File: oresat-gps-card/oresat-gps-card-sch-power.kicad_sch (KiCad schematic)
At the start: 97 parts, among them Q1 DMP2240UDM, Q2 PMV45EN, Q3 DMP3050LVT-7, Q4 DMP3050LVT-7, Q5 PMV45EN, U2 MAX7310ATE, U3 MIC842LYC5, U4 MIC842LYC5, U5 MAX4211FETE, U6 LTC3624, U7 TS5A21366

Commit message: Routine Push
First attempt to clean up schematic
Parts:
- added C51: 10n, Capacitor_SMD:C_1210_3225Metric, symbol Device:C
- added C52: 470n, Capacitor_SMD:C_1210_3225Metric, symbol Device:C
- added R49, R50: 10k, Resistor_SMD:R_0603_1608Metric, symbol Device:R_US
- R24: value 4.7k -> 2.7k
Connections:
- net CB_CTRL: now also R49.1; no longer Q4.3 (G), R39.1
- net VBUSP: now also C52.1
- net at Q4.4 (S), R32.2, R39.2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: now also C51.1
- new net: C51.2, Q4.3 (G), R39.1, R49.2, R50.2
- new net: C52.2, R50.1
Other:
- note added: "Do we need this?"
- moved on the sheet: Q5, R39, R40

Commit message: Routine Push
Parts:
- added D11: GREEN, LED_SMD:LED_0603_1608Metric, symbol Device:LED
- added R61: 10k, Resistor_SMD:R_0603_1608Metric, symbol Device:R_US
- C1, C2, C8: footprint Capacitor_SMD:C_0805_2012Metric -> Capacitor_SMD:C_0603_1608Metric
- C13, C14, C51, C52, C6: footprint Capacitor_SMD:C_1210_3225Metric -> Capacitor_SMD:C_0603_1608Metric
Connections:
- net GND: now also D11.1 (K)
- net ON/~{OFF}: now also R61.1
- new net: D11.2 (A), R61.2
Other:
- note added: "All resistors are 0603 1% AEC-Q200 unless marked. All capacitors are 0603 AEC-Q200 Vw >= 16V X5R or better unless marked."
- note added: "Main Power Switch Vbus = (6.0,7.2,8.4)V"
- note added: "OreSat Power Domain (OPD) Power Supply (3.3V) Address 0011001 or 19"
- note removed: "Main Power Switch"
- note removed: "OreSat Power Domain (OPD) Controller"
- note removed: "OreSat Power Domain (OPD) Power Supply (3.3V)"
- note removed: "Vbus = (6.0,7.2,8.4)V"

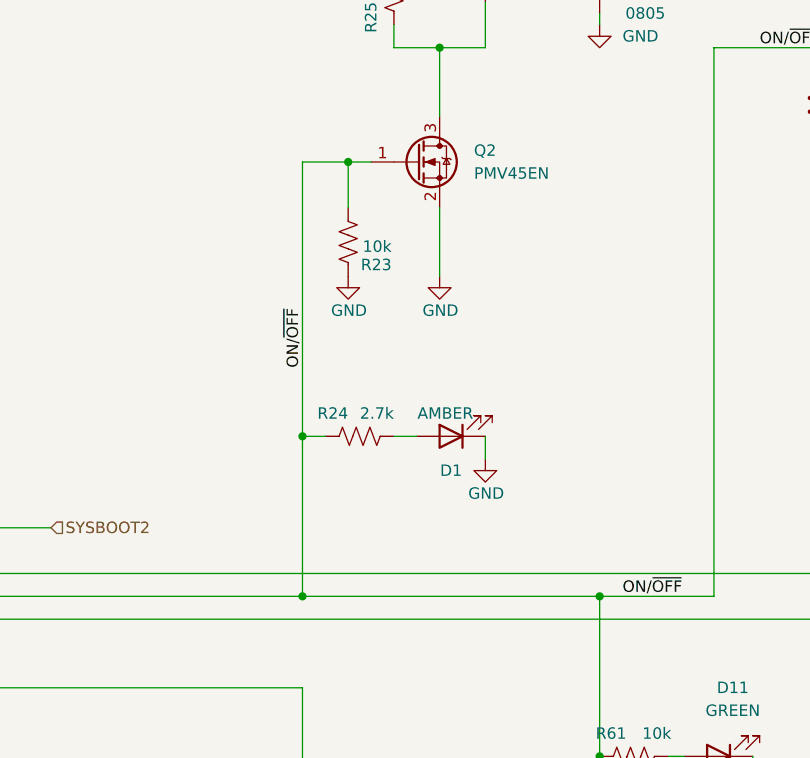
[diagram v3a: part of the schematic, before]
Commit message: Cleaned up silkscreen
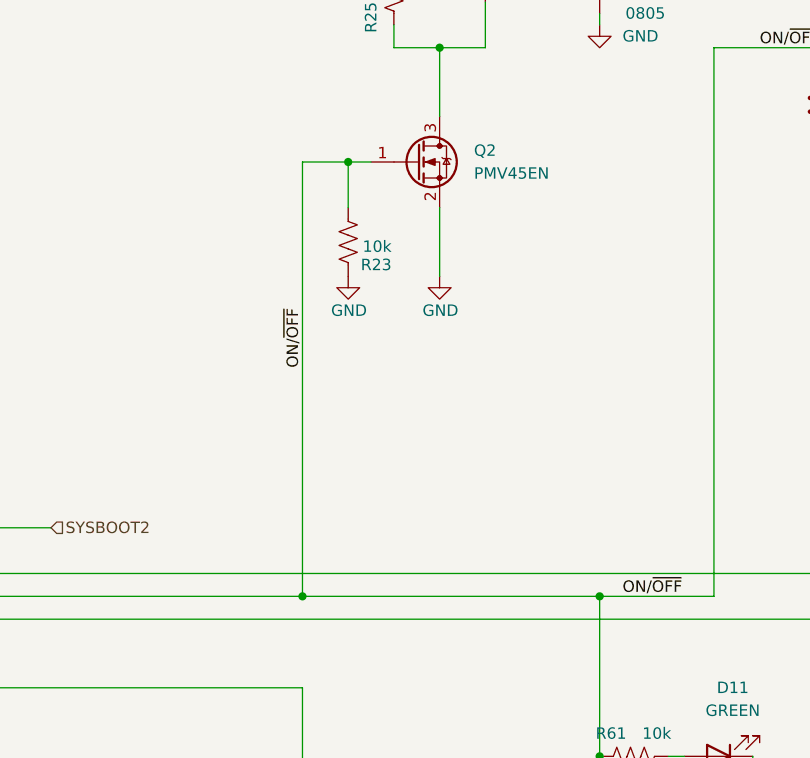
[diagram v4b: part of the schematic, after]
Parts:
- removed D1: AMBER, LED_SMD:LED_0603_1608Metric, symbol Device:LED
- removed R24: 2.7k, Resistor_SMD:R_0603_1608Metric, symbol Device:R_US

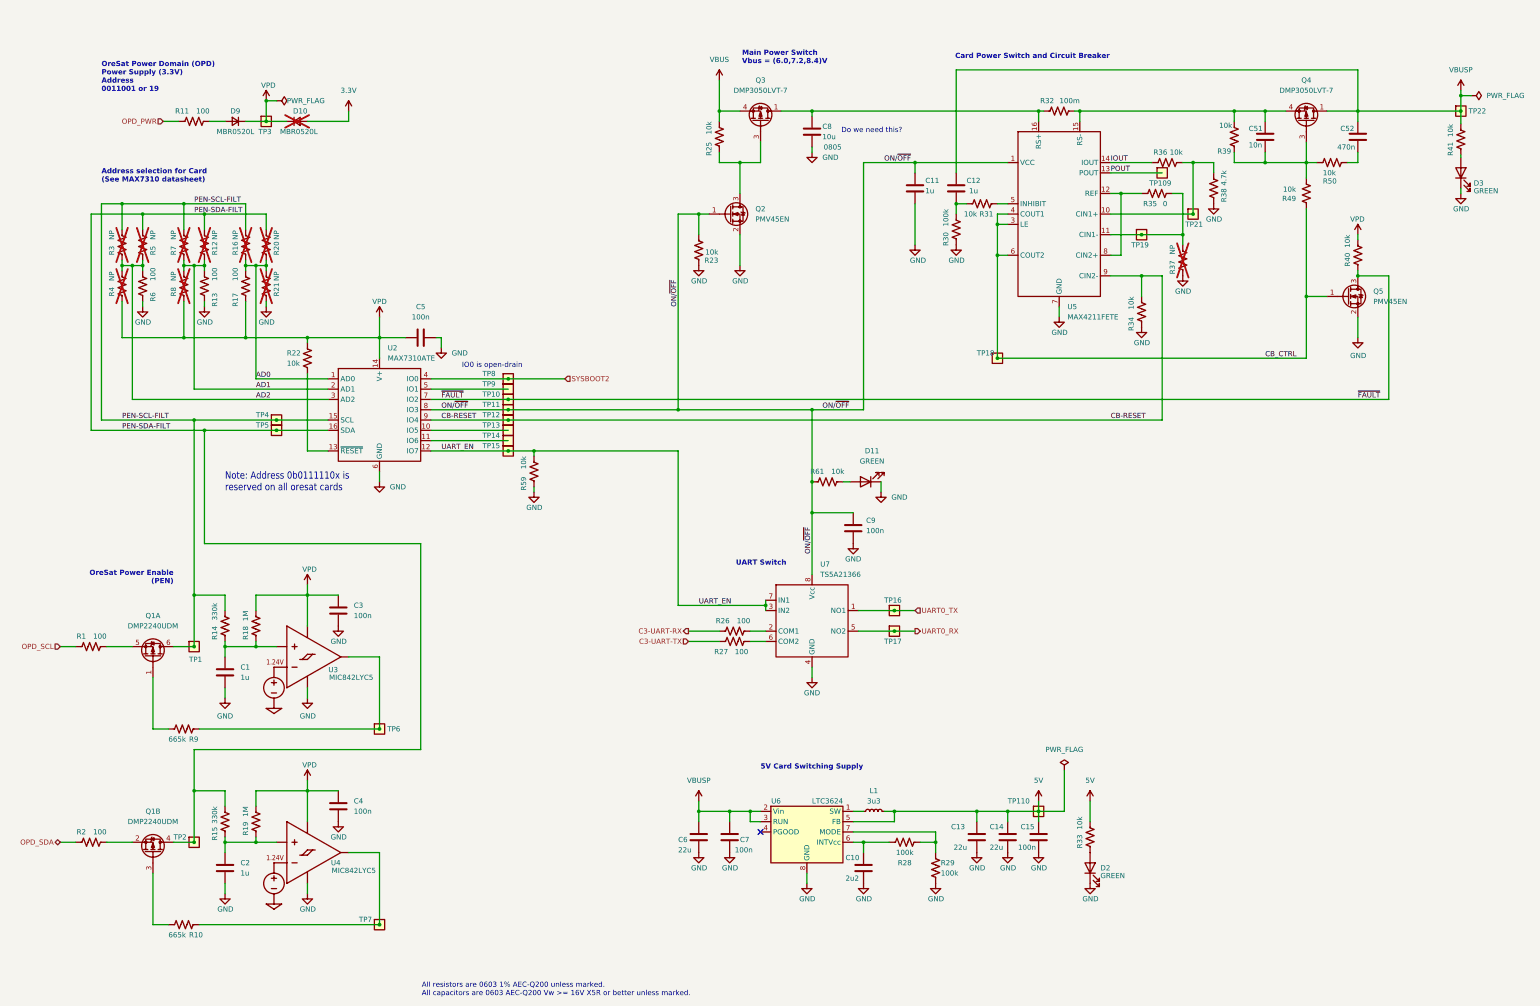
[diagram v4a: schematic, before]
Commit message: General cleanup of schematic and layout
Updated .gitignore, updates DRU file, moved RF lines to RF-50-MIN (max is just too big),
lots of cleanup on the root page to make it pretty, cleaned up some redudant labels,
updated SMPM connector and added rule zone, updated PCB outline to include NPTH drills
for SMPM connectors, began cleanup of OPD.
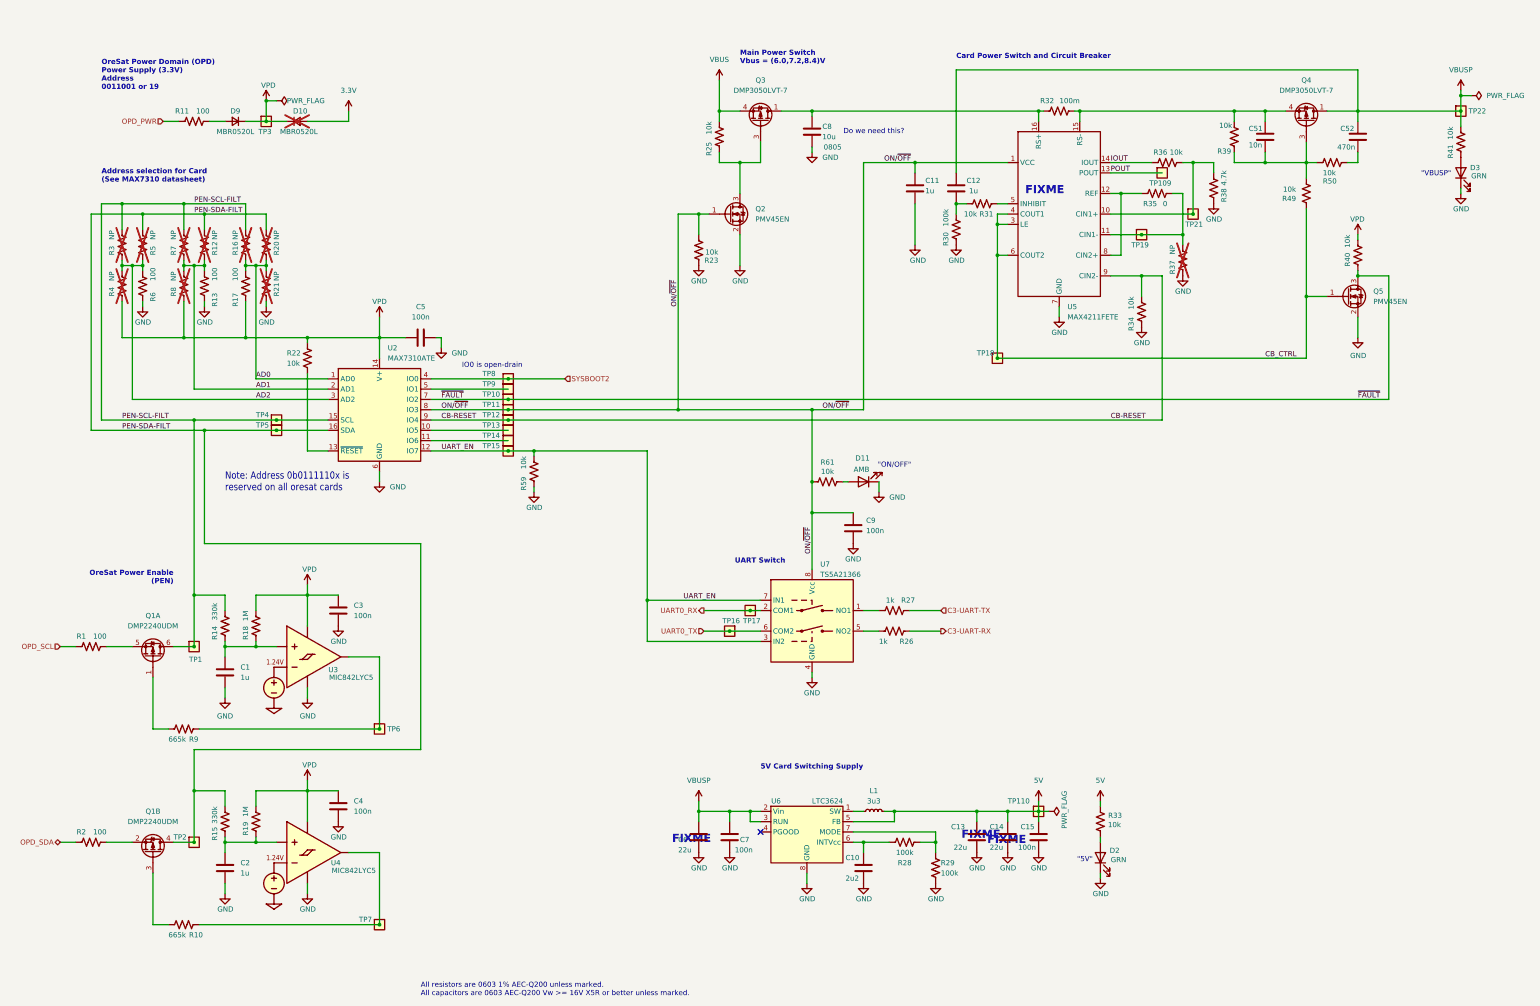
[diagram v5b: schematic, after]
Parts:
- D11: value GREEN -> AMB
- D2, D3: value GREEN -> GRN
- R26, R27: value 100 -> 1k
- U7: DIS (none) -> DigiKey; DPN (none) -> 296-24304-1-ND; MFR (none) -> Texas Instruments; MPN (none) -> TS5A21366DCUR
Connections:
- net UART0_RX: now also U7.2 (COM1); no longer U7.5 (NO2)
- net UART0_TX: now also U7.6 (COM2); no longer U7.1 (NO1)
- net at R26.2: now also U7.5 (NO2); no longer U7.2 (COM1)
- net at R27.1: now also U7.1 (NO1); no longer U7.6 (COM2)
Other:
- note added: ""5V""
- note added: ""ON/OFF""
- note added: ""VBUSP""
- note added: "FIXME"
- moved on the sheet: D11, D2, R26, R27, R33, R41, TP16, TP17

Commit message: Routine Push
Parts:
- removed C11, C12: 1u, Capacitor_SMD:C_0603_1608Metric, symbol Device:C
- removed C13, C14, C6: 22u, Capacitor_SMD:C_0603_1608Metric, symbol Device:C
- removed C51: 10n, Capacitor_SMD:C_0603_1608Metric, symbol Device:C
- removed C52: 470n, Capacitor_SMD:C_0603_1608Metric, symbol Device:C
- removed C8: 10u, Capacitor_SMD:C_0603_1608Metric, symbol Device:C
- removed C9: 100n, Capacitor_SMD:C_0603_1608Metric, symbol Device:C
- removed D11: AMB, LED_SMD:LED_0603_1608Metric, symbol Device:LED
- removed D3: GRN, LED_SMD:LED_0603_1608Metric, symbol Device:LED
- removed Q2, Q5: PMV45EN, oresat-ics:SOT23, symbol Device:Q_NMOS_GSD
- removed Q3, Q4: DMP3050LVT-7, Package_TO_SOT_SMD:SOT-23-6, symbol oresat-transistors:DMP3050LVT-7
- removed R23, R25, R31, R34, R36, R39, R40, R41, R49, R50, R61: 10k, Resistor_SMD:R_0603_1608Metric, symbol Device:R_US
- removed R26, R27: 1k, Resistor_SMD:R_0603_1608Metric, symbol Device:R_US
- removed R30: 100k, Resistor_SMD:R_0603_1608Metric, symbol Device:R_US
- removed R32: 100m, Resistor_SMD:R_1206_3216Metric, symbol Device:R_US
- removed R35: 0, Resistor_SMD:R_0603_1608Metric, symbol Device:R_US
- removed R37: NP, Resistor_SMD:R_0603_1608Metric, symbol Device:R_US
- removed R38: 4.7k, Resistor_SMD:R_0603_1608Metric, symbol Device:R_US
- removed TP109, TP16, TP17, TP18, TP19, TP21, TP22: 1x01, oresat-misc:TestPoint-0.75mm-th, symbol oresat-misc:Test-Point-0.75mm-th
- removed U5: MAX4211FETE, Package_DFN_QFN:QFN-16-1EP_4x4mm_P0.65mm_EP2.1x2.1mm, symbol oresat-ics:MAX4211FETE
- removed U7: TS5A21366, Package_SO:VSSOP-8_2.3x2mm_P0.5mm, symbol oresat-ics:TS5A21366
- added C59: 10u, oresat-passives:0805-B-NOSILK, symbol Device:C
- added C60, C62: 1u, oresat-passives:0603-C-NOSILK, symbol Device:C_Small
- added C61: 100n, oresat-passives:0603-C-NOSILK, symbol Device:C_Small
- added C63: 10n, oresat-passives:0603-C-NOSILK, symbol Device:C_Small
- added C64: 470n, oresat-passives:0603-C-NOSILK, symbol Device:C_Small
- added D13: AMBER, LED_SMD:LED_0603_1608Metric, symbol Device:LED_Small_Filled
- added D5: GRN, LED_SMD:LED_0603_1608Metric, symbol Device:LED_Small_Filled
- added Q10, Q11: DMP3050LVT-7, Package_TO_SOT_SMD:TSOT-23-6, symbol oresat-transistors:DMP3050LVT-7
- added Q12, Q8: PMV45EN, Package_TO_SOT_SMD:SOT-23, symbol Transistor_FET:Q_NMOS_GSD
- added R100, R103, R104, R105, R106, R107, R108, R64, R93, R97, R98: 10k, oresat-passives:0603-C-NOSILK, symbol Device:R_US
- added R101, R102: 0, oresat-passives:0603-C-NOSILK, symbol Device:R_US
- added R109: 2.7k, oresat-passives:0603-C-NOSILK, symbol Device:R_US
- added R92, R94, R95: 1k, oresat-passives:0603-C-NOSILK, symbol Device:R_US
- added R96: 100k, oresat-passives:0603-C-NOSILK, symbol Device:R_US
- added R99: 100m, Resistor_SMD:R_1206_3216Metric, symbol Device:R_US
- added TP33, TP34, TP35, TP36, TP37, TP38, TP39, TP40, TP41, TP42: Test-Point, oresat-misc:TestPoint-0.75mm-th, symbol oresat-misc:Test-Point-0.75mm-th
- added U20: TS5A21366DCUR, Package_SO:VSSOP-8_2.3x2mm_P0.5mm, symbol oresat-ics:TS5A21366
- added U21: MAX4211FETE, Package_DFN_QFN:QFN-16-1EP_4x4mm_P0.65mm_EP2.1x2.1mm, symbol oresat-ics:MAX4211D/E/F
- C7: value 100n -> 10u
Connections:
- net C3-UART-RX: now also R94.1
- net C3-UART-TX: now also R95.1
- net CB-RESET: now also R100.2, TP38.1, U21.9 (CIN2-)
- net CB_CTRL: now also Q12.1 (G), R106.1, TP39.1, U21.3 (LE), U21.4 (COUT1), U21.6 (COUT2)
- net GND: now also C59.2, C60.2, C61.1, D13.1 (K), D5.1 (K), Q12.2 (S), Q8.2 (S), R100.1, R103.1, R104.1, R93.1, R96.1, R97.2, U20.4 (GND), U21.17 (GND), U21.7 (GND)
- net UART_EN: now also U20.3 (IN2), U20.7 (IN1)
- net VBUS: now also Q10.4 (S), R64.2
- net VBUSP: now also C62.2, C64.2, Q11.1 (D), Q11.2 (D), Q11.5 (D), Q11.6 (D), R109.2, TP42.1
- net VPD: now also R108.2
- net ~{FAULT}: now also Q12.3 (D), R108.1, TP41.1
- net at TP9.1, U2.5 (IO1): now also TP33.1
- net ON/~{OFF} renamed ON/~{OFF}
- net ON/~{OFF}: now also C60.1, C61.2, Q8.1 (G), R92.1, R93.2, TP34.1, U20.8 (Vcc), U21.1 (VCC)
- net SYSBOOT2: no longer names the net of TP8.1, U2.4 (IO0)
- net SYSBOOT2: now also TP36.1
- new net: C64.1, R107.1
- new net: R97.1, U21.2 (IN)
- new net: C63.1, Q11.3 (G), R105.1, R106.2, R107.2
- new net: C63.2, Q11.4 (S), R105.2, R99.2, U21.15 (RS-)
- new net: R102.1, R104.2, TP40.1, U21.10 (CIN1+)
- new net: R101.1, R103.2, TP37.1, U21.11 (CIN1-)
- new net: R101.2, U21.12 (REF), U21.8 (CIN2+)
- new net: TP35.1, U21.13 (POUT)
- new net: C59.1, Q10.1 (D), Q10.2 (D), Q10.5 (D), Q10.6 (D), R99.1, U21.16 (RS+)
- new net: R98.1, U21.5 (INHIBIT)
- new net: C62.1, R96.2, R98.2
- new net: Q10.3 (G), Q8.3 (D), R64.1
- new net: D13.2 (A), R92.2
- new net: D5.2 (A), R109.1
- new net: R94.2, U20.1 (NO1)
- new net: R95.2, U20.5 (NO2)
- new net 411-IOUT: R102.2, U21.14 (IOUT)
- new net MCU-UART-RX: U20.6 (COM2)
- new net MCU-UART-TX: U20.2 (COM1)
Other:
- note added: ""ON/!OFF""
- note added: "0805"
- note added: "1206"
- note added: "250 ms inhibit on power up"
- note added: "C3-UART signals protected when IC unpowered"
- note added: "Circuit breaker switch with ~10 ms soft start"
- note added: "Feedback settings trips at 295m mA"
- note added: "Main Power Switch"
- note added: "ON/~{OFF} signal powers MAX4211 + TS5A Saves quiescent OPD power draw"
- note added: "TX/RX CROSS IS DONE HERE"
- note added: "UART switch"
- note added: "Vbus = (6.0,7.2,8.4)V"
- note removed: ""ON/OFF""
- note removed: "Do we need this?"
- note removed: "FIXME"
- note removed: "Main Power Switch Vbus = (6.0,7.2,8.4)V"
- note removed: "UART Switch"
- moved on the sheet: C15, C7, D2, R28, R29, R33, TP110
